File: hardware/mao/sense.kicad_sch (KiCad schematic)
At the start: 14 parts, among them U401 LSM6DSOXTR, U402 VL53L4CDV0DH/1, U403 OPT3004DNPR

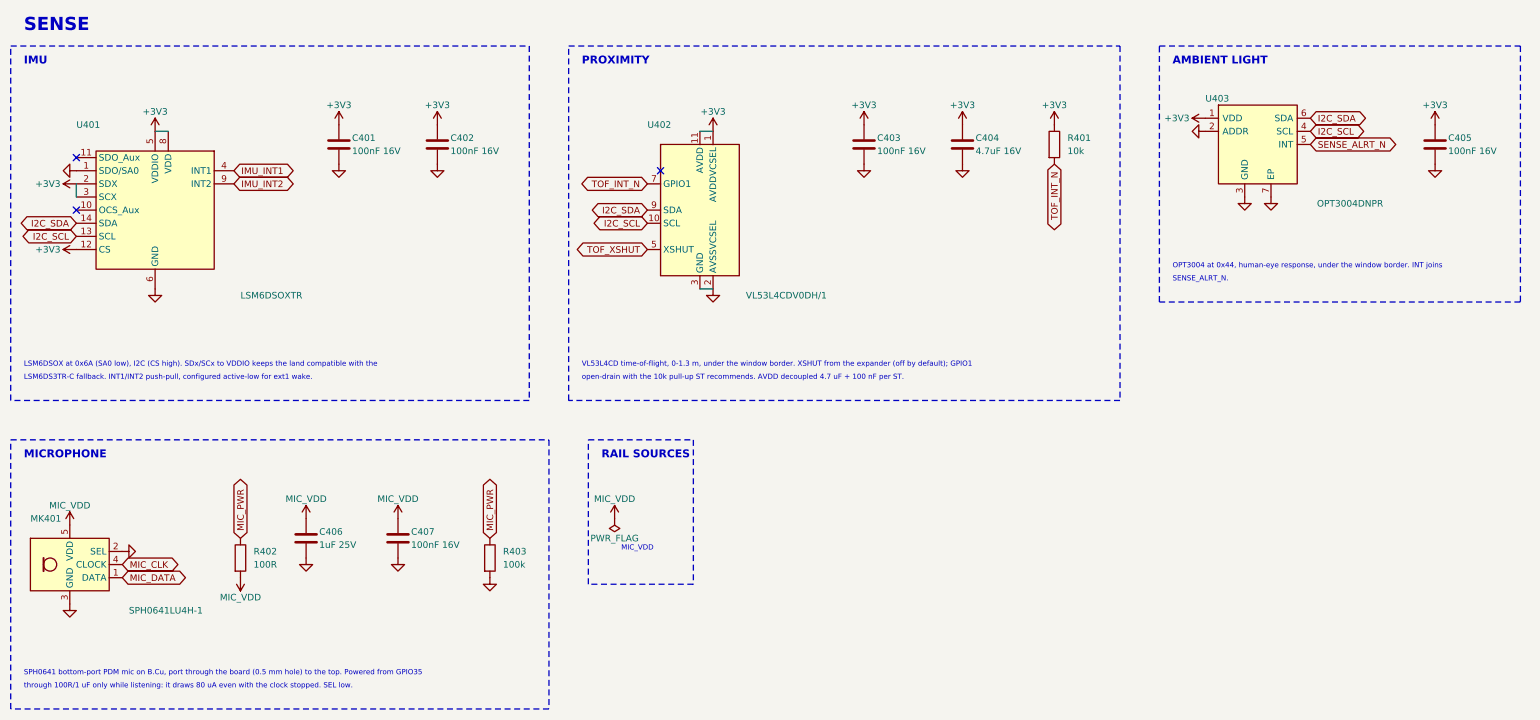
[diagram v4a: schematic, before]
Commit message: A1 capture: Gate C architecture on the A0 puck (schematic, ERC 0)
circuit.py now describes MAO_MAIN A1 (ERC 0 at all severities, 137 parts, 75 nets):
- ESP32-S3-MINI-1-N8 on RF_Module:ESP32-S2-MINI-1 (Gate C land audit); GPIO0 = BOOT pad only
  (10k + TP8), GPIO3/45/46 NC, 22R + DNP 10 pF on USB at the module, VBUS_SENSE 100k/150k.
- BQ25185 (ILIM/VSET 18k: 4.2 V / 500 mA; ISET 1.43k: 210 mA as A0; TS/MR to the NTC, DNP 10k,
  TSMR pad; /CE 100k pull-down; STAT1/2 10k to +3V3) replaces BQ24073.
- TPS62840 (VSET 102k = 3.2 V, SLVSEC6D table 1; 2.2 uH, CIN 4.7 uF, COUT 10 uF; MODE/STOP low,
  EN to VIN) replaces TPS63802 and its UVLO/FB dividers; LINK_REG 0R added, LINK_BAT kept.
- ICM-42670-P replaces LSM6DSOX on the same land (0x68, INT1 100k pull-up, INT2 not wired).
- DRV2605L VDD and pin 6 on +3V3; constant-current backlight sink (TLV9061 + DMG2302UK, 3.3R)
  replaces the AW9364; TPS22916C for the panel rail and the IR receiver rail.
- MAX98357A SD_MODE straight from GPIO9 (2.2k series dropped: +3V3 <= VSYS by topology).
- Removed: touch (4 zones, electrodes, springs), SPH0641, OPT3004, TCA6408A, board-ID divider.
- I2C pull-ups 4.7k; new fixture pads BL, AMP, TE, PRS, HLA, TSMR, CE, IO21, IO26.
- Battery connector stays JST SH: the Gate C JST PH side entry is 4.8 mm tall (KiCad STEP of the
  PH side-entry housing) against the 3.2 mm B-side zone over the cell; owner decision.
Parts kept from A0 keep their references; removed numbers are retired.
New footprint MAO:TI_DLC0008B_VSON-HR-8 (TI land example 4224310/A, from the Gate C generator);
A0-only custom footprints removed. Board name MAO_MAIN_A1; A0 board/outputs removed from this tree
(they stay on the A0 branch).

Co-Authored-By: Claude Opus 5.5 <noreply@anthropic.com>
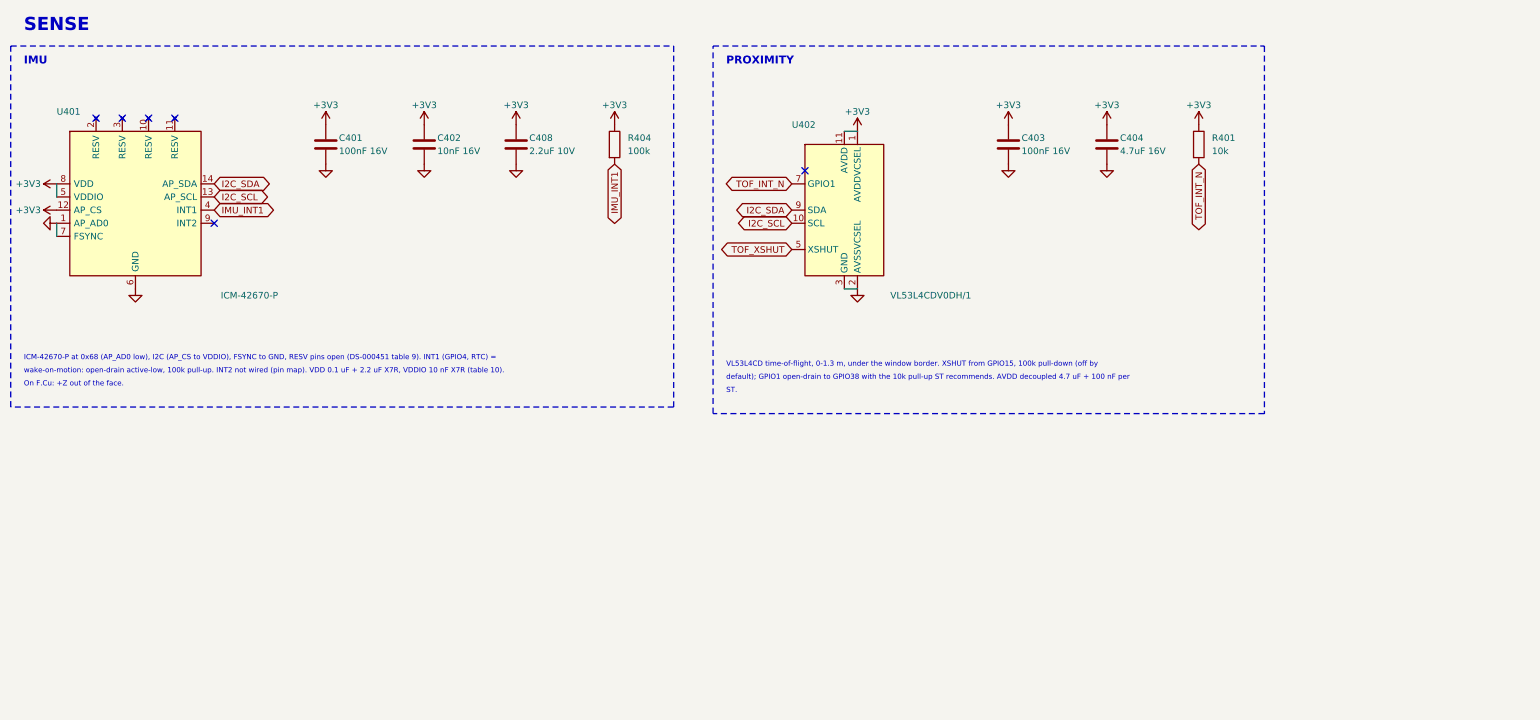
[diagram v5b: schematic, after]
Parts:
- removed C405, C407: 100nF 16V, Capacitor_SMD:C_0402_1005Metric, symbol Device:C
- removed C406: 1uF 25V, Capacitor_SMD:C_0402_1005Metric, symbol Device:C
- removed MK401: SPH0641LU4H-1, Sensor_Audio:Knowles_LGA-5_3.5x2.65mm, symbol Sensor_Audio:SPH0641LU4H-1
- removed R402: 100R, Resistor_SMD:R_0402_1005Metric, symbol Device:R
- removed R403: 100k, Resistor_SMD:R_0402_1005Metric, symbol Device:R
- removed U403: OPT3004DNPR, MAO:TI_DNP0006A_USON-6_2x2mm_P0.65mm_EP0.65x1.35mm, symbol MAO:OPT3004
- added C408: 2.2uF 10V, Capacitor_SMD:C_0603_1608Metric, symbol Device:C
- added R404: 100k, Resistor_SMD:R_0402_1005Metric, symbol Device:R
- C402: value 100nF 16V -> 10nF 16V; LCSC C1525 -> C318577; MPN CL05B104KO5NNNC -> CL05B103KO5NNNC
- U401: value LSM6DSOXTR -> ICM-42670-P; symbol MAO:LSM6DSOX -> MAO:ICM-42670-P; LCSC C481766 -> C3288646; MPN LSM6DSOXTR -> ICM-42670-P; Manufacturer ST -> TDK InvenSense
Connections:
- net +3V3: now also C408.1, R404.1; no longer U401.2 (SDX), U401.3 (SCX)
- net GND: now also C408.2
- net IMU_INT1: now also R404.2
- net IMU_INT2: no longer names the net of U401.9 (INT2)
- no-connect marks 3 -> 6
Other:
- note added: "ICM-42670-P at 0x68 (AP_AD0 low), I2C (AP_CS to VDDIO), FSYNC to GND, RESV pins open (DS-000451 table 9). INT1 (GPIO4, RTC) ="
- note added: "On F.Cu: +Z out of the face."
- note added: "ST."
- note added: "VL53L4CD time-of-flight, 0-1.3 m, under the window border. XSHUT from GPIO15, 100k pull-down (off by"
- note added: "default); GPIO1 open-drain to GPIO38 with the 10k pull-up ST recommends. AVDD decoupled 4.7 uF + 100 nF per"
- note added: "wake-on-motion: open-drain active-low, 100k pull-up. INT2 not wired (pin map). VDD 0.1 uF + 2.2 uF X7R, VDDIO 10 nF X7R (table 10)."
- note removed: "AMBIENT LIGHT"
- note removed: "LSM6DS3TR-C fallback. INT1/INT2 push-pull, configured active-low for ext1 wake."
- note removed: "LSM6DSOX at 0x6A (SA0 low), I2C (CS high). SDx/SCx to VDDIO keeps the land compatible with the"
- note removed: "MICROPHONE"
- note removed: "MIC_VDD"
- note removed: "OPT3004 at 0x44, human-eye response, under the window border. INT joins"
- note removed: "RAIL SOURCES"
- note removed: "SENSE_ALRT_N."
- note removed: "SPH0641 bottom-port PDM mic on B.Cu, port through the board (0.5 mm hole) to the top. Powered from GPIO35"
- note removed: "VL53L4CD time-of-flight, 0-1.3 m, under the window border. XSHUT from the expander (off by default); GPIO1"
- note removed: "open-drain with the 10k pull-up ST recommends. AVDD decoupled 4.7 uF + 100 nF per ST."
- note removed: "through 100R/1 uF only while listening: it draws 80 uA even with the clock stopped. SEL low."
- title: MAO_MAIN A0 - Sense -> MAO_MAIN A1 - Sense
- moved on the sheet: C401, C402, C403, C404, R401, U402

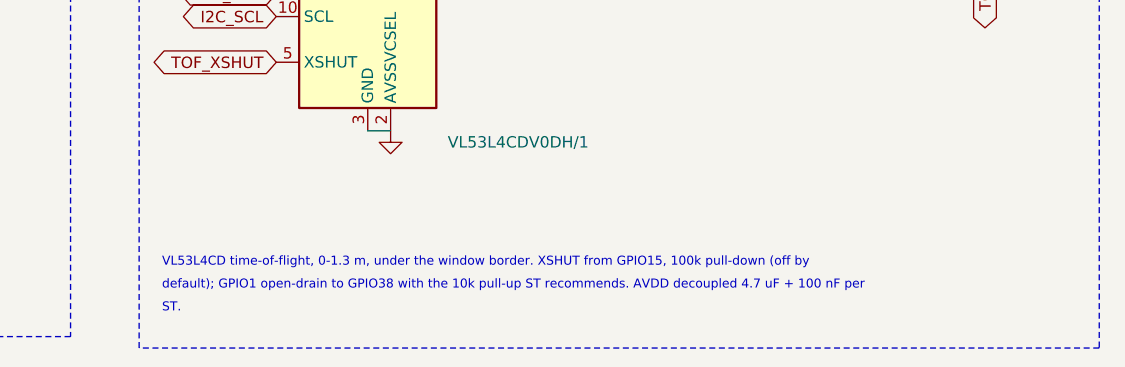
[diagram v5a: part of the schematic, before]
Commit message: A1 capture/layout follow the pin swaps (ERC 0); escapes and fixture pads moved with their nets
Co-Authored-By: Claude Opus 5.5 <noreply@anthropic.com>
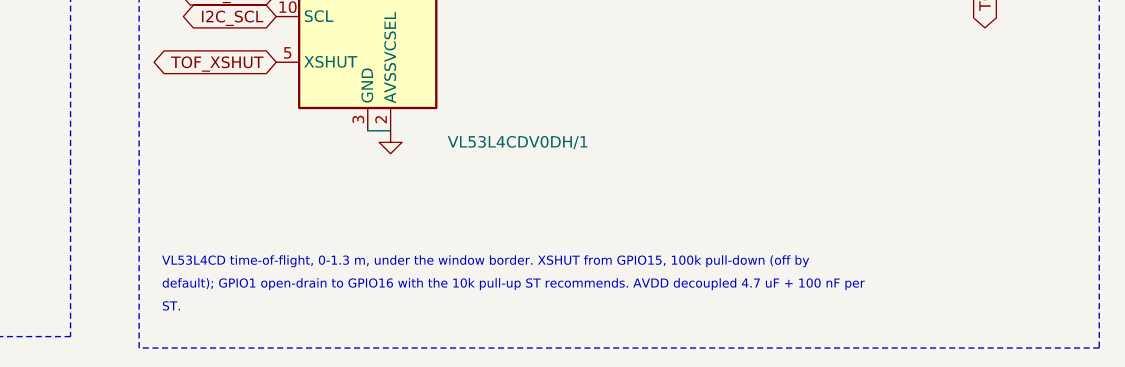
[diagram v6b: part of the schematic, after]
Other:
- note added: "default); GPIO1 open-drain to GPIO16 with the 10k pull-up ST recommends. AVDD decoupled 4.7 uF + 100 nF per"
- note removed: "default); GPIO1 open-drain to GPIO38 with the 10k pull-up ST recommends. AVDD decoupled 4.7 uF + 100 nF per"
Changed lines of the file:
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@@
 		)
 	)
-	(text "default); GPIO1 open-drain to GPIO38 with the 10k pull-up ST recommends. AVDD decoupled 4.7 uF + 100 nF per"
+	(text "default); GPIO1 open-drain to GPIO16 with the 10k pull-up ST recommends. AVDD decoupled 4.7 uF + 100 nF per"
 		(exclude_from_sim no)
 		(at 151.13 85.09 0)

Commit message: A1 routed: DRC 0 / unconnected 0 / parity 0, planes continuous, silk/mech/stack-up checks clean, fab package
- Board: grid-router pass 10 (79 of 80 nets) + route_finish (AMP_LRCLK, four boxed GND pads incl. R117.2's
  pour island) + prune/stitch/tidy/offpad/snap45. kicad-cli DRC: 0 violations, 0 unconnected, 0 parity;
  plane_check: GND, VBUS, VSYS, +3V3 one piece each; ERC 0 (98 fitted + 5 DNP, 75 nets).
- silk.py / mao_labels.py: relaunch with subprocess instead of os.execv (Windows split the KiCad python path at
  its space and the silk pass silently did nothing); face identity moved to 3 o'clock (A1's escape vias took
  A0's spot), IMU axes scan for the nearest clear field, the back mark leaves the battery pin cues room.
  check_silk_text: 74 texts, 0 findings. mech_check: 137 parts, 0 findings.
- C402 fields synced to the Basic 10 nF part (sync_fields), schematic regenerated.
- outputs/fab: gerbers (12) + drill (4) + zip, JLC BOM 47 lines / 98 parts with sourcing columns, off-board
  LCSC list, CPL 98 rows, assembly drawings; layer plots and renders in docs/hardware.

Co-Authored-By: Claude Opus 5.5 <noreply@anthropic.com>
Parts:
- C402: value 10nF 16V -> 10nF 50V; LCSC C318577 -> C15195; MPN CL05B103KO5NNNC -> CL05B103KB5NNNC
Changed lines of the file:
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@@
 			)
 		)
-		(property "Value" "10nF 16V"
+		(property "Value" "10nF 50V"
 			(at 95.25 40.64 0)
 			(effects
@@
 			)
 		)
-		(property "MPN" "CL05B103KO5NNNC"
+		(property "MPN" "CL05B103KB5NNNC"
 			(at 92.71 39.37 0)
 			(effects
@@
 			)
 		)
-		(property "LCSC" "C318577"
+		(property "LCSC" "C15195"
 			(at 92.71 39.37 0)
 			(effects
